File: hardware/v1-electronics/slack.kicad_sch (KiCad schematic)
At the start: 0 parts

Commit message: checkpoint(v1 hardware): this is the save before corrections
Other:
- note added: "- Check circuits - I don't know if my circuit actually needs seperate power and digital grounds. Schematic - [x] Refactor Schematic to r/PrintedCircuitBoard Guide - [x] Refactor the root schematic to show how the system is connected - I want to add logic levels and ground differentiation - I want custom grapics for each symbol - [-] Refactor chip configurations to explain my choices - [x] Rename 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"
- note removed: "- Compare charger ICs - Check circuits - Choose passive conponent values - Connect the LED and Switch matrices. Assign LEDs to each inputs. - Select PCB foot prints I feel that my power and ground levels are confusing Schematic - [] Refactor Schematic to r/PrintedCircuitBoard Guide - [x] Refactor the root schematic to show how the system is connected - I want to add logic levels and ground differ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"
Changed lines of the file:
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@@
 	(title_block
 		(title "Slack")
-		(date "2026-06-17")
-		(rev "A.0.0")
+		(date "2026-07-12")
+		(rev "A.0.3")
 	)
 	(rectangle
-		(start -104.14 40.64)
-		(end -2.54 215.9)
+		(start 15.24 124.46)
+		(end 106.68 200.66)
 		(stroke
 			(width 0.5)
@@
 	(text "Loose Notes"
 		(exclude_from_sim no)
-		(at -101.6 43.18 0)
+		(at 17.78 127 0)
 		(effects
 			(font
@@
 	(text "KiCad Feature Requests:\nHierarchical Bus\nHierarchical Sheet Symbols"
 		(exclude_from_sim no)
-		(at -101.6 106.68 0)
+		(at 17.78 190.5 0)
 		(effects
 			(font
@@
 		)
 	)
-	(text "- Compare charger ICs\n- Check circuits\n- Choose passive conponent values\n- Connect the LED and Switch matrices. Assign LEDs to each inputs.\n- Select PCB foot prints\n\nI feel that my power and ground levels are confusing\n\nSchematic\n- [] Refactor Schematic to r/PrintedCircuitBoard Guide\n- [x] Refactor the root schematic to show how the system is connected\n	- I want to add logic levels and ground differentiation\n	- I want custom grapics for each symbol\n- [-] Refactor chip configurations to explain my choices\n- [] Rename all the component references so they are grouped and easier to layout\n- [] Select actual components, footprints, 3D models for all components\n- [] Pass those design reviews softwares\n\nPCB\n- generate and recreate ergonomic montary key layout in PCB\n- determine latch layout on PCB"
+	(text "- Check circuits\n- I don't know if my circuit actually needs\n  seperate power and digital grounds.\n\nSchematic\n- [x] Refactor Schematic to r/PrintedCircuitBoard Guide\n- [x] Refactor the root schematic to show how the system is connected\n	- I want to add logic levels and ground differentiation\n	- I want custom grapics for each symbol\n- [-] Refactor chip configurations to explain my choices\n- [x] Rename all the component references so they are\n     grouped and easier to layout\n- [] Select actual components, footprints, 3D models for all components\n- [x] Pass those design reviews softwares\n- [] take review advice\n\nPCB\n- generate and recreate ergonomic montary key layout in PCB\n- determine latch layout on PCB"
 		(exclude_from_sim no)
-		(at -101.6 53.34 0)
+		(at 17.78 137.16 0)
 		(effects
 			(font
@@
 	(text ""
 		(exclude_from_sim no)
-		(at -86.36 106.68 0)
+		(at 33.02 190.5 0)
 		(effects
 			(font

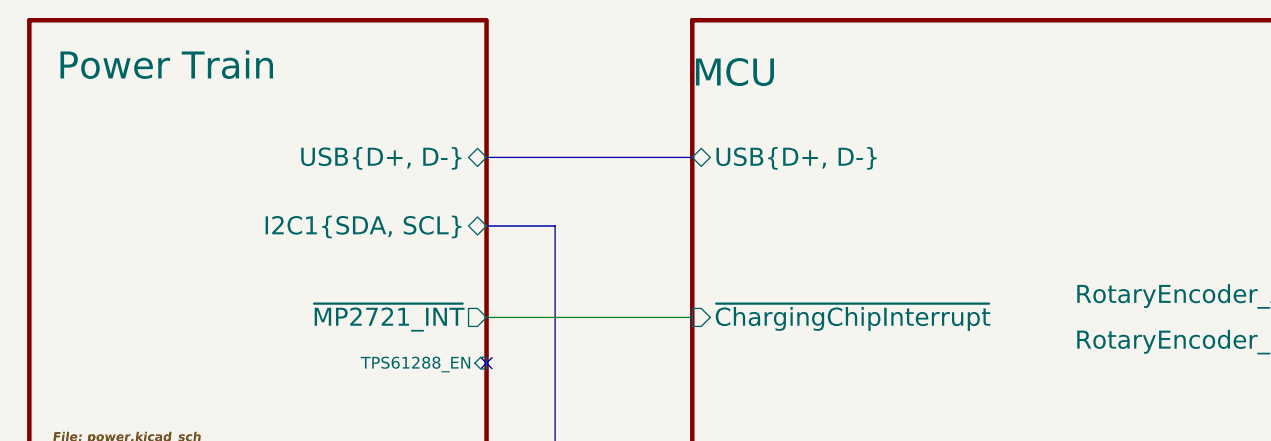
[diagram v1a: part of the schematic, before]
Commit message: fix(v1 hardware): implementing recommendations from Cyril
- rated the lines for the power system
- using a properly rated connecter for the battery
- added manual usb cc detection
- short grounds to each other
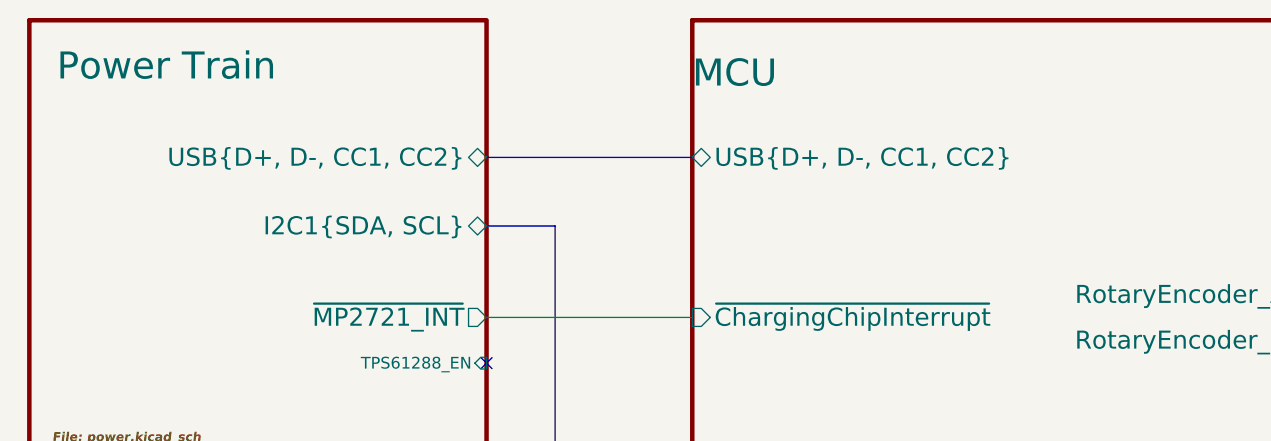
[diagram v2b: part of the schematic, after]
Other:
- sheet MCU ports: added USB{D+, D-, CC1, CC2}; removed USB{D+, D-}
- sheet Power Train ports: added USB{D+, D-, CC1, CC2}; removed USB{D+, D-}
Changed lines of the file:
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@@
 	(title_block
 		(title "Slack")
-		(date "2026-07-12")
-		(rev "A.0.3")
+		(date "2026-07-25")
+		(rev "A.0.4")
 	)
 	(rectangle
@@
 			)
 		)
-		(pin "USB{D+, D-}" bidirectional
+		(pin "USB{D+, D-, CC1, CC2}" bidirectional
 			(at 66.04 40.64 0)
 			(effects
@@
 			)
 		)
-		(pin "USB{D+, D-}" bidirectional
+		(pin "USB{D+, D-, CC1, CC2}" bidirectional
 			(at 88.9 40.64 180)
 			(effects

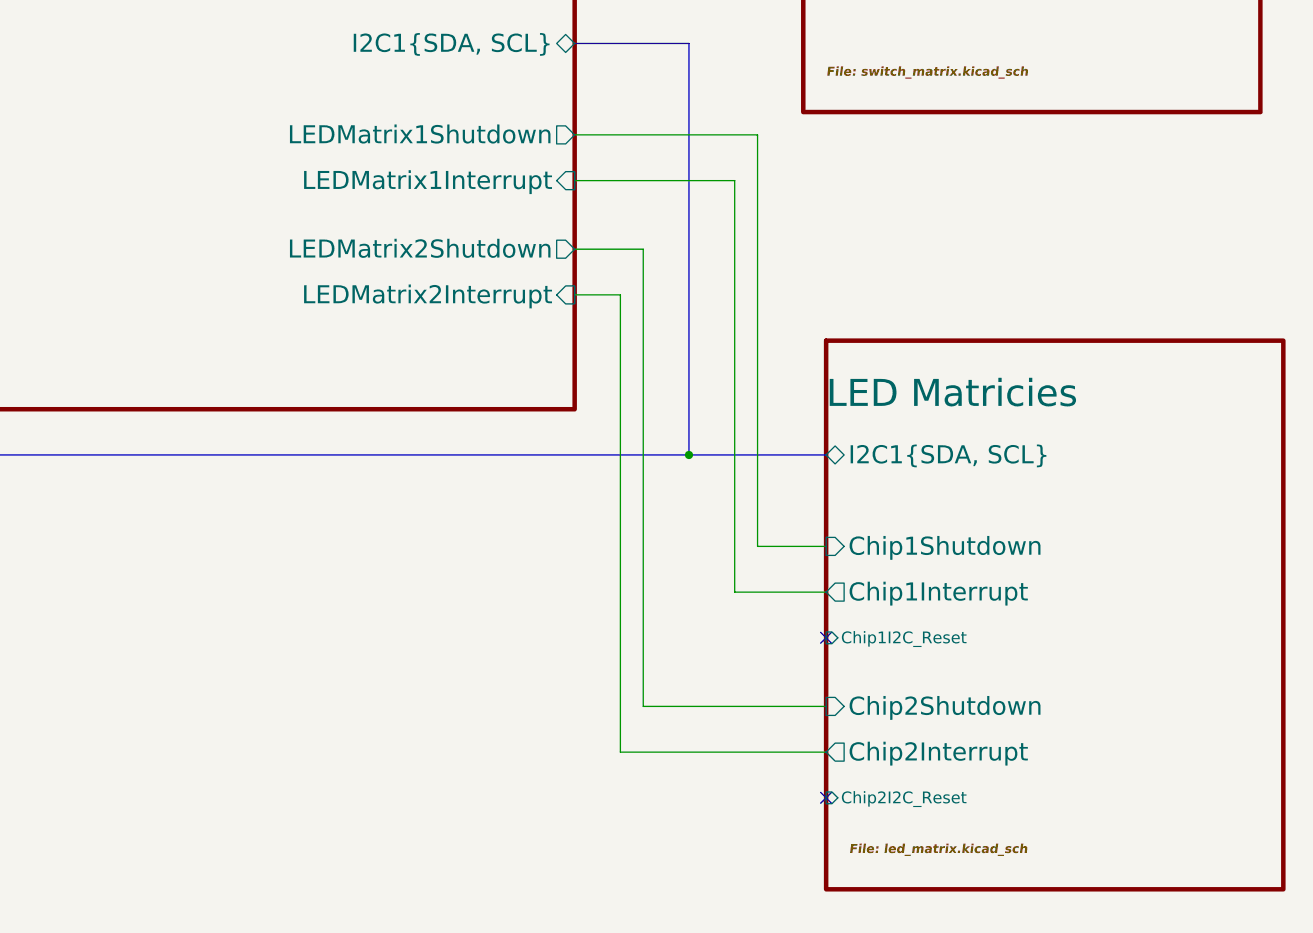
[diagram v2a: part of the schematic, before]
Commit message: fix(v1 hardware): complete set of recommendations
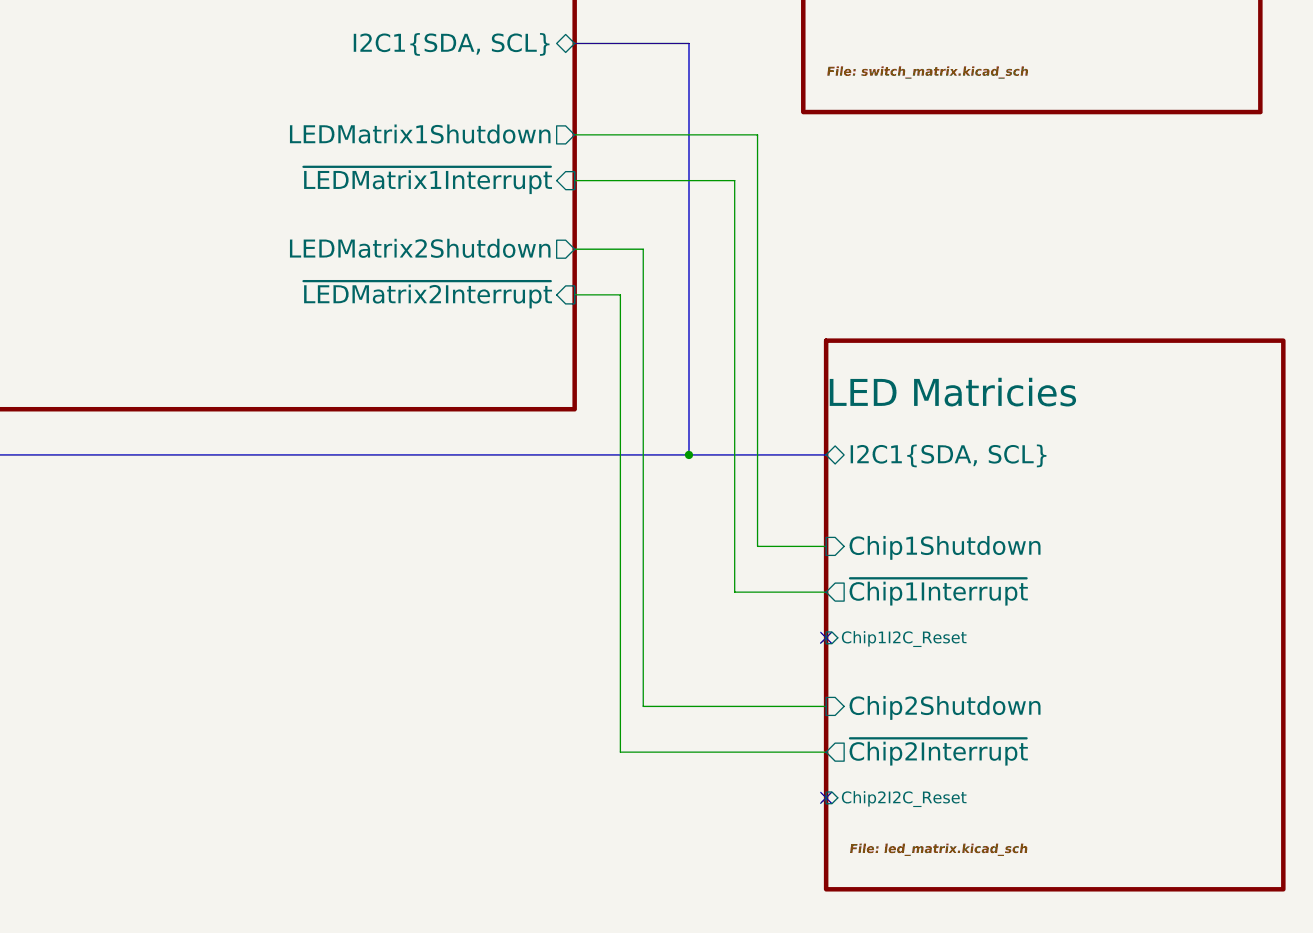
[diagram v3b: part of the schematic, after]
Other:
- sheet LED Matricies ports: added ~{Chip1Interrupt}, ~{Chip2Interrupt}; removed Chip1Interrupt, Chip2Interrupt
- sheet MCU ports: added ~{LEDMatrix1Interrupt}, ~{LEDMatrix2Interrupt}; removed LEDMatrix1Interrupt, LEDMatrix2Interrupt
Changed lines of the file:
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@@
 			)
 		)
-		(pin "LEDMatrix1Interrupt" input
+		(pin "~{LEDMatrix1Interrupt}" input
 			(at 177.8 83.82 0)
 			(effects
@@
 			)
 		)
-		(pin "LEDMatrix2Interrupt" input
+		(pin "~{LEDMatrix2Interrupt}" input
 			(at 177.8 96.52 0)
 			(effects
@@
 			)
 		)
-		(pin "Chip1Interrupt" output
+		(pin "~{Chip1Interrupt}" output
 			(at 205.74 129.54 180)
 			(effects
@@
 			)
 		)
-		(pin "Chip2Interrupt" output
+		(pin "~{Chip2Interrupt}" output
 			(at 205.74 147.32 180)
 			(effects
